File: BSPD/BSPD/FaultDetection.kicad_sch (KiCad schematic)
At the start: 15 parts, among them U10 LM397, U11 LM397, U12 LM397, U13 74AHC1G32, U14 74AHC1G32, U15 74AHC1G32, U9 LM397

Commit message: Relay Driver/Regulator/IO/LEDS/Comparator
Added relay driver, 5v regulator, debugging leds, 6 pin microfit connector for IO, and created footprint for TLV7012DDFR comparator we're using
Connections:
- net Brake Over: now reaches U13.1, U9.4
- net Brake Under: now reaches U10.4, U13.2
- net Current Over: now reaches U11.4, U14.1
- net Current Under: now reaches U12.4, U14.2
- net Current Sense: now reaches U12.3 (+)
- net Current Sense: now also U11.3 (+)
- net Brake Sense: now reaches U9.3 (+)
- net Brake Sense: now also U10.3 (+)
- net Circuit Fault: now reaches U15.4
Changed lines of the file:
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@@
 		)
 	)
-	(netclass_flag ""
-		(length 2.54)
-		(shape round)
-		(at 39.37 106.68 90)
+	(label "Brake Over"
+		(at 77.47 40.64 0)
+		(fields_autoplaced yes)
 		(effects
 			(font
@@
 			(justify left bottom)
 		)
-		(property "Netclass" "Sense2"
-			(at 31.496 103.378 0)
-			(effects
-				(font
-					(size 2 2)
-					(italic yes)
-				)
-				(justify left)
+	)
+	(label "Current Sense"
+		(at 39.37 139.7 180)
+		(fields_autoplaced yes)
+		(effects
+			(font
+				(size 1.8 1.8)
 			)
+			(justify right)
 		)
 	)
-	(netclass_flag ""
-		(length 2.54)
-		(shape round)
-		(at 39.37 139.7 90)
+	(label "Circuit Fault"
+		(at 158.75 90.17 0)
+		(fields_autoplaced yes)
 		(effects
 			(font
@@
 			(justify left bottom)
 		)
-		(property "Netclass" "Sense2"
-			(at 31.496 136.398 0)
-			(effects
-				(font
-					(size 2 2)
-					(italic yes)
-				)
-				(justify left)
+	)
+	(label "Brake Sense"
+		(at 39.37 38.1 180)
+		(fields_autoplaced yes)
+		(effects
+			(font
+				(size 1.8 1.8)
 			)
+			(justify right)
+		)
+	)
+	(label "Current Under"
+		(at 77.47 142.24 0)
+		(fields_autoplaced yes)
+		(effects
+			(font
+				(size 1.27 1.27)
+			)
+			(justify left top)
+		)
+	)
+	(label "Current Over"
+		(at 77.47 109.22 0)
+		(fields_autoplaced yes)
+		(effects
+			(font
+				(size 1.27 1.27)
+			)
+			(justify left bottom)
+		)
+	)
+	(label "Current Sense"
+		(at 39.37 106.68 180)
+		(fields_autoplaced yes)
+		(effects
+			(font
+				(size 1.8 1.8)
+			)
+			(justify right)
+		)
+	)
+	(label "Brake Under"
+		(at 77.47 73.66 0)
+		(fields_autoplaced yes)
+		(effects
+			(font
+				(size 1.27 1.27)
+			)
+			(justify left top)
+		)
+	)
+	(label "Brake Sense"
+		(at 39.37 71.12 180)
+		(fields_autoplaced yes)
+		(effects
+			(font
+				(size 1.8 1.8)
+			)
+			(justify right)
 		)
 	)
@@
 		(length 2.54)
 		(shape round)
-		(at 158.75 90.17 270)
-		(effects
-			(font
-				(size 1.27 1.27)
-			)
-			(justify right bottom)
-		)
-		(property "Netclass" "CircuitFault"
-			(at 160.528 92.71 0)
-			(effects
-				(font
-					(size 1.27 1.27)
-					(italic yes)
-				)
-				(justify left)
-			)
-		)
-	)
-	(netclass_flag ""
-		(length 2.54)
-		(shape round)
 		(at 49.53 96.52 0)
 		(fields_autoplaced yes)
@@
 					(italic yes)
 				)
-				(justify left)
-			)
-		)
-	)
-	(netclass_flag ""
-		(length 2.54)
-		(shape round)
-		(at 39.37 71.12 90)
-		(effects
-			(font
-				(size 1.27 1.27)
-			)
-			(justify left bottom)
-		)
-		(property "Netclass" "Sense1"
-			(at 31.496 67.818 0)
-			(effects
-				(font
-					(size 2 2)
-					(italic yes)
-				)
-				(justify left)
-			)
-		)
-	)
-	(netclass_flag ""
-		(length 2.54)
-		(shape round)
-		(at 39.37 38.1 90)
-		(effects
-			(font
-				(size 1.27 1.27)
-			)
-			(justify left bottom)
-		)
-		(property "Netclass" "Sense1"
-			(at 31.496 34.798 0)
-			(effects
-				(font
-					(size 2 2)
-					(italic yes)
-				)

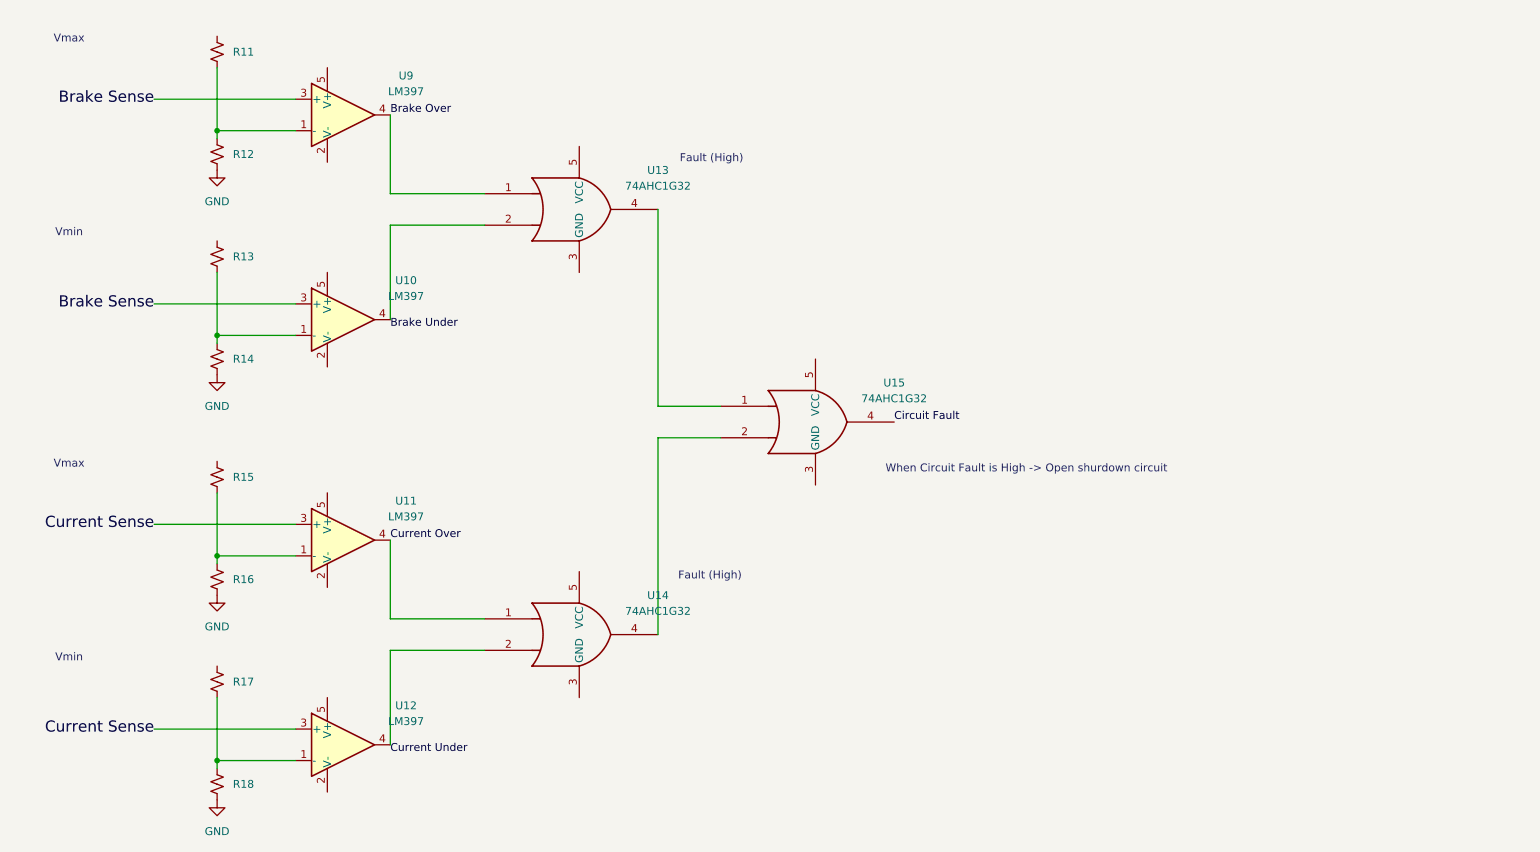
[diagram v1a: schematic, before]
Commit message: Added logic gate symbols
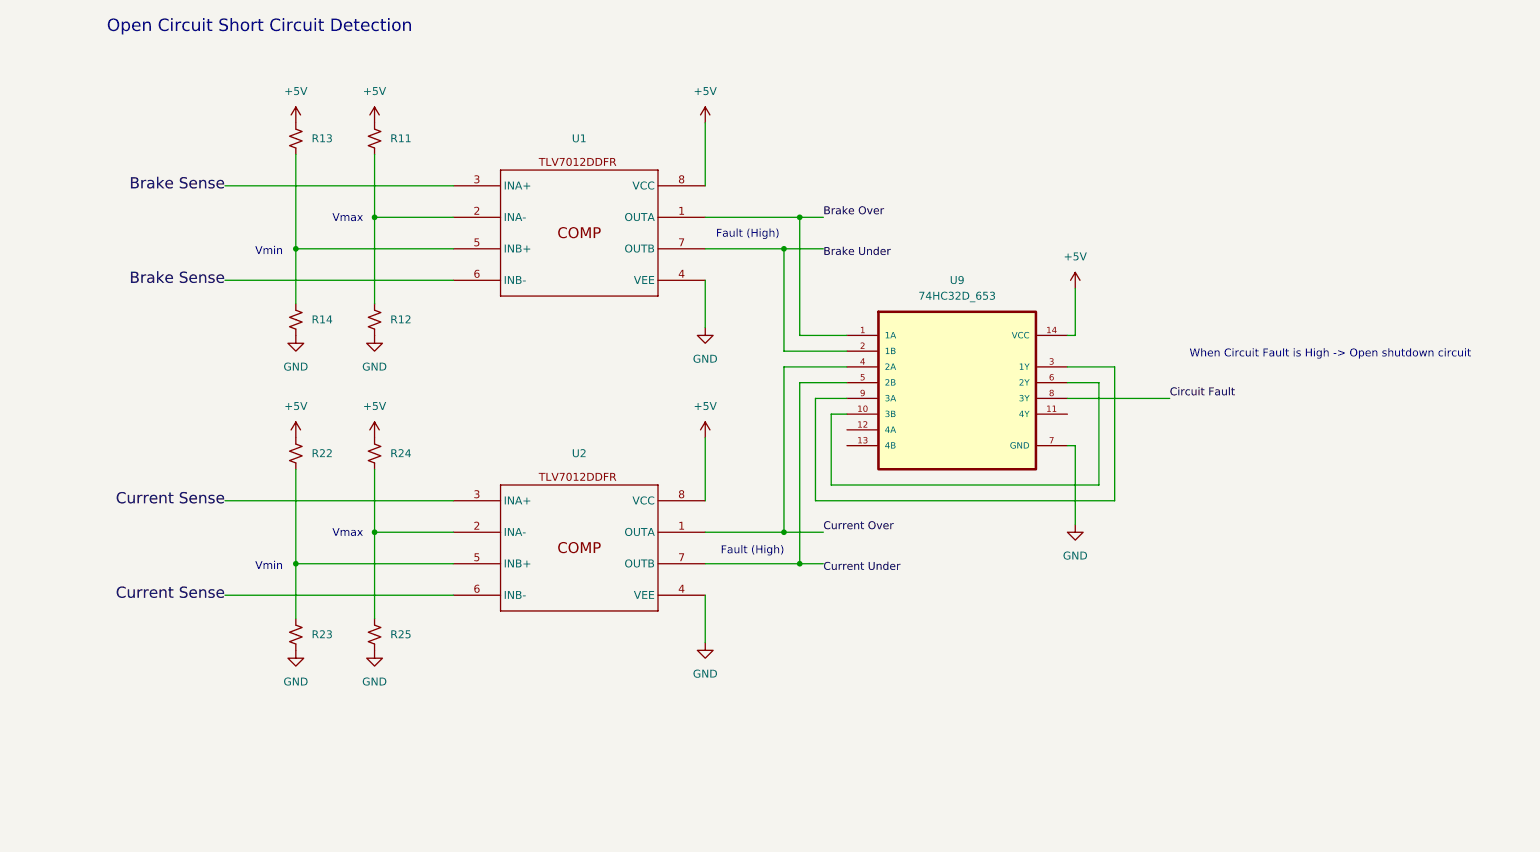
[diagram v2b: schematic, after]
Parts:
- removed R15, R16, R17, R18: R_Small_US, symbol Device:R_Small_US
- removed U10, U11, U12, U9: LM397, Package_TO_SOT_SMD:SOT-23-5, symbol Comparator:LM397
- removed U13, U14, U15: 74AHC1G32, symbol 74xGxx:74AHC1G32
- added R22, R23, R24, R25: R_Small_US, symbol Device:R_Small_US
- added U1, U2: ~, symbol TLV7012DDFR:TLV7012DDFR
- added U9: 74HC32D_653, 74HC32D_653:SOIC127P600X175-14N, symbol 74HC32D_653:74HC32D_653
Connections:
- net Brake Over: now also U1.1 (OUTA), U9.1 (1A)
- net Brake Sense: now also U1.3 (INA+), U1.6 (INB-)
- net Brake Under: now also U1.7 (OUTB), U9.2 (1B)
- net Circuit Fault: now also U9.8 (3Y)
- net Current Over: now also U2.1 (OUTA), U9.4 (2A)
- net Current Sense: now also U2.3 (INA+), U2.6 (INB-)
- net Current Under: now also U2.7 (OUTB), U9.5 (2B)
- net GND: now also R23.2, R25.2, U1.4 (VEE), U2.4 (VEE), U9.7 (GND)
- net at R13.2, R14.1: now also U1.5 (INB+)
- net at R11.2, R12.1: now also U1.2 (INA-)
- net +5V: now reaches R13.1
- net +5V: now also R11.1, R22.1, R24.1, U1.8 (VCC), U2.8 (VCC), U9.14 (VCC)
- new net: R22.2, R23.1, U2.5 (INB+)
- new net: U9.10 (3B), U9.6 (2Y)
- new net: U9.3 (1Y), U9.9 (3A)
- new net: R24.2, R25.1, U2.2 (INA-)
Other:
- note added: "Open Circuit Short Circuit Detection"
- note added: "When Circuit Fault is High -> Open shutdown circuit"
- note removed: "When Circuit Fault is High -> Open shurdown circuit"
- moved on the sheet: R11, R12, R13, R14

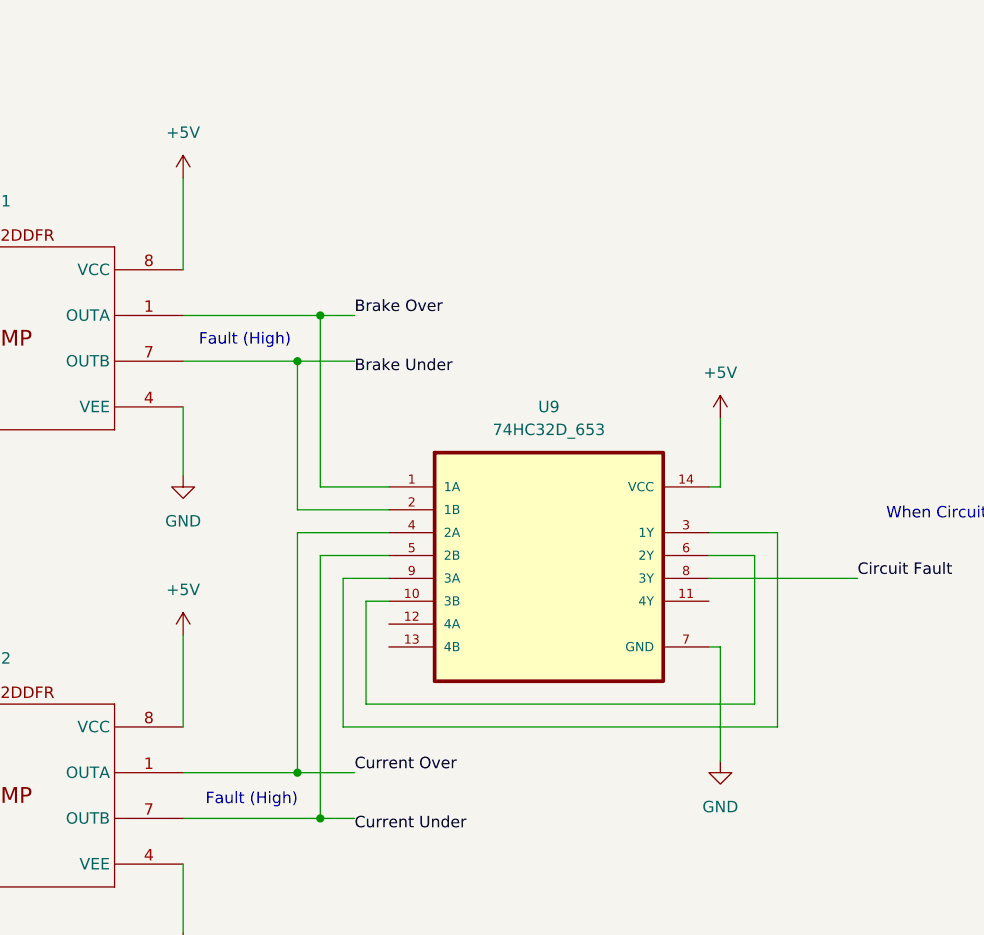
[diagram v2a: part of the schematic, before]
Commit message: Added decoupling caps
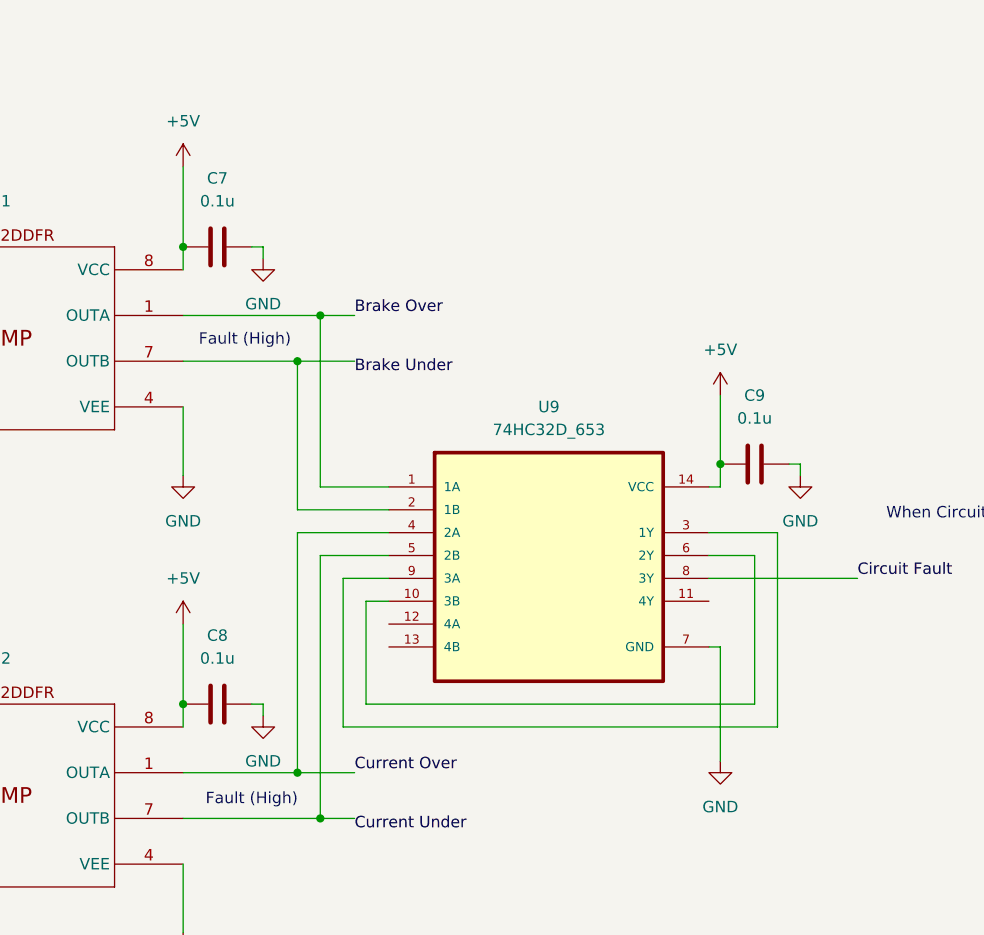
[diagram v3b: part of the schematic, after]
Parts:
- added C7, C8, C9: 0.1u, symbol Device:C
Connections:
- net +5V: now also C7.1, C8.1, C9.1
- net GND: now also C7.2, C8.2, C9.2

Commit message: Configured footprints and set board outline.
All footprints have been assigned to the components, and the board size and it's mounting holes have been set up in the pcb editor.
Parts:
- C7, C8, C9: footprint (none) -> CL10A104K:CAP_CL10_SAM
- R11, R12, R13, R14, R22, R23, R24, R25: footprint (none) -> Resistor_SMD:R_0603_1608Metric_Pad0.98x0.95mm_HandSolder
- U1, U2: footprint (none) -> Package_TO_SOT_SMD:SOT-23-8
- U9: footprint 74HC32D_653:SOIC127P600X175-14N -> Package_SO:SO-14_5.3x10.2mm_P1.27mm
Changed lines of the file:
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@@
 			)
 		)
-		(property "Footprint" ""
+		(property "Footprint" "CL10A104K:CAP_CL10_SAM"
 			(at 195.58 72.6948 0)
 			(effects
@@
 			)
 		)
-		(property "Footprint" ""
+		(property "Footprint" "Resistor_SMD:R_0603_1608Metric_Pad0.98x0.95mm_HandSolder"
 			(at 62.23 95.25 0)
 			(effects
@@
 			)
 		)
-		(property "Footprint" "74HC32D_653:SOIC127P600X175-14N"
+		(property "Footprint" "Package_SO:SO-14_5.3x10.2mm_P1.27mm"
 			(at 168.91 87.63 0)
 			(effects
@@
 			)
 		)
-		(property "Footprint" ""
+		(property "Footprint" "Resistor_SMD:R_0603_1608Metric_Pad0.98x0.95mm_HandSolder"
 			(at 74.93 95.25 0)
 			(effects
@@
 			)
 		)
-		(property "Footprint" ""
+		(property "Footprint" "Resistor_SMD:R_0603_1608Metric_Pad0.98x0.95mm_HandSolder"
 			(at 62.23 73.66 0)
 			(effects
@@
 			)
 		)
-		(property "Footprint" ""
+		(property "Footprint" "Package_TO_SOT_SMD:SOT-23-8"
 			(at 95.25 59.69 0)
 			(effects
@@
 			)
 		)
-		(property "Footprint" ""
+		(property "Footprint" "CL10A104K:CAP_CL10_SAM"
 			(at 135.89 48.5648 0)
 			(effects
@@
 			)
 		)
-		(property "Footprint" ""
+		(property "Footprint" "CL10A104K:CAP_CL10_SAM"
 			(at 135.89 99.3648 0)
 			(effects
@@
 			)
 		)
-		(property "Footprint" ""
+		(property "Footprint" "Resistor_SMD:R_0603_1608Metric_Pad0.98x0.95mm_HandSolder"
 			(at 74.93 124.46 0)
 			(effects
@@
 			)
 		)
-		(property "Footprint" ""
+		(property "Footprint" "Package_TO_SOT_SMD:SOT-23-8"
 			(at 95.25 110.49 0)
 			(effects
@@
 			)
 		)
-		(property "Footprint" ""
+		(property "Footprint" "Resistor_SMD:R_0603_1608Metric_Pad0.98x0.95mm_HandSolder"
 			(at 62.23 44.45 0)
 			(effects
@@
 			)
 		)
-		(property "Footprint" ""
+		(property "Footprint" "Resistor_SMD:R_0603_1608Metric_Pad0.98x0.95mm_HandSolder"
 			(at 62.23 124.46 0)
 			(effects
@@
 			)
 		)
-		(property "Footprint" ""
+		(property "Footprint" "Resistor_SMD:R_0603_1608Metric_Pad0.98x0.95mm_HandSolder"
 			(at 74.93 73.66 0)
 			(effects
@@
 			)
 		)
-		(property "Footprint" ""
+		(property "Footprint" "Resistor_SMD:R_0603_1608Metric_Pad0.98x0.95mm_HandSolder"
 			(at 74.93 44.45 0)
 			(effects
